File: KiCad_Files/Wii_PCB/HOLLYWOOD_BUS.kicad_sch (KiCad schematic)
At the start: 5 parts

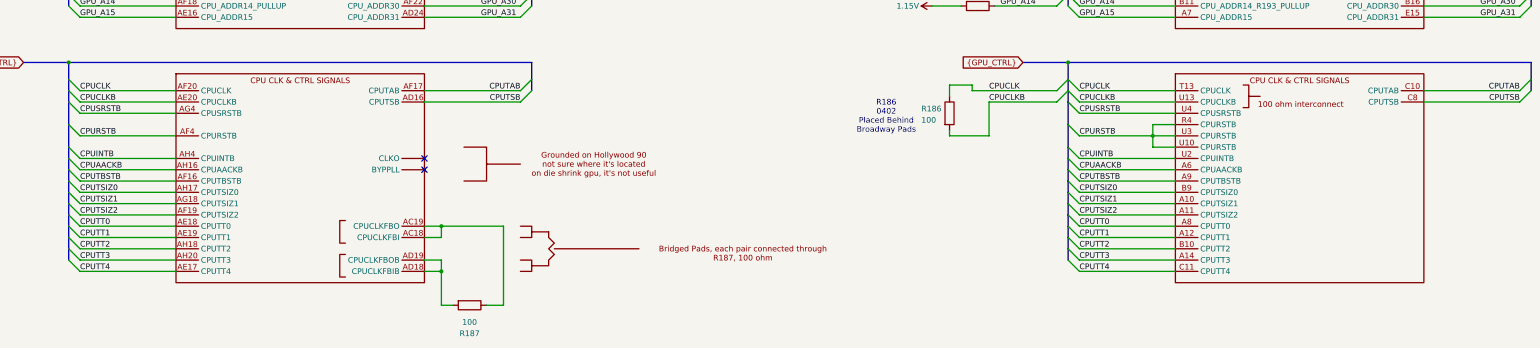
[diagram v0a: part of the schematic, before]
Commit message: Updated RAM & GPU bus to allow custom net rules for measuring intra-track spacing, added pad for reset, removed debug pads, reorganized ram schematic to cluster length matched signals, changed MX chip and U10 symbols, and re-labeled the wifi net interface.
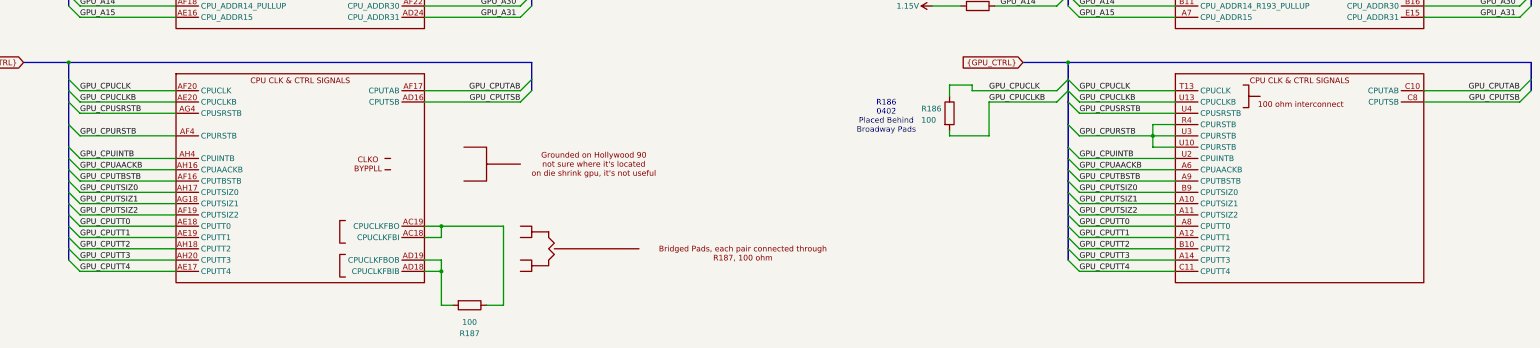
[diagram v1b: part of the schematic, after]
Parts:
- BROADWAY1: footprint wii_bgaLibrary:Updated BROADWAY -> WeeWii_Library:Updated BROADWAY
- HOLLYWOOD1: footprint wii_bgaLibrary:Updated HOLLYWOOD -> WeeWii_Library:Updated HOLLYWOOD
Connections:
- net CPUAACKB renamed GPU_CPUAACKB
- net CPUCLK renamed GPU_CPUCLK
- net CPUCLKB renamed GPU_CPUCLKB
- net CPUINTB renamed GPU_CPUINTB
- net CPURSTB renamed GPU_CPURSTB
- net CPUSRSTB renamed GPU_CPUSRSTB
- net CPUTAB renamed GPU_CPUTAB
- net CPUTBSTB renamed GPU_CPUTBSTB
- net CPUTSB renamed GPU_CPUTSB
- net CPUTSIZ0 renamed GPU_CPUTSIZ0
- net CPUTSIZ1 renamed GPU_CPUTSIZ1
- net CPUTSIZ2 renamed GPU_CPUTSIZ2
- net CPUTT0 renamed GPU_CPUTT0
- net CPUTT1 renamed GPU_CPUTT1
- net CPUTT2 renamed GPU_CPUTT2
- net CPUTT3 renamed GPU_CPUTT3
- net CPUTT4 renamed GPU_CPUTT4
- no-connect marks 2 -> 0
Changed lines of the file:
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@@
 	(paper "A3")
 	(bus_alias "GPU_CTRL"
-		(members "CPUCLK" "CPUCLKB" "CPUSRSTB" "CPURSTB" "CPUINTB" "CPUAACKB" "CPUTBSTB"
-			"CPUTSIZ0" "CPUTSIZ1" "CPUTSIZ2" "CPUTT0" "CPUTT1" "CPUTT2" "CPUTT3" "CPUTT4"
-			"CPUTAB" "CPUTSB"
+		(members "GPU_CPUCLK" "GPU_CPUCLKB" "GPU_CPUSRSTB" "GPU_CPURSTB" "GPU_CPUINTB"
+			"GPU_CPUAACKB" "GPU_CPUTBSTB" "GPU_CPUTSIZ0" "GPU_CPUTSIZ1" "GPU_CPUTSIZ2"
+			"GPU_CPUTT0" "GPU_CPUTT1" "GPU_CPUTT2" "GPU_CPUTT3" "GPU_CPUTT4" "GPU_CPUTAB"
+			"GPU_CPUTSB"
 		)
 	)
@@
 		(color 0 0 0 0)
 	)
-	(no_connect
-		(at 132.08 222.25)
-	)
-	(no_connect
-		(at 132.08 224.79)
-	)
 	(bus_entry
 		(at 378.46 180.34)
@@
 		)
 	)
-	(label "CPUTSB"
+	(label "GPU_CPUTSB"
 		(at 378.46 209.55 180)
 		(effects
@@
 		)
 	)
-	(label "CPUTSIZ2"
+	(label "GPU_CPUTSIZ2"
 		(at 279.4 234.95 0)
 		(effects
@@
 		)
 	)
-	(label "CPUTT4"
+	(label "GPU_CPUTT4"
 		(at 54.61 247.65 0)
 		(effects
@@
 		)
 	)
-	(label "CPUTBSTB"
+	(label "GPU_CPUTBSTB"
 		(at 54.61 227.33 0)
 		(effects
@@
 		)
 	)
-	(label "CPUAACKB"
+	(label "GPU_CPUAACKB"
 		(at 279.4 224.79 0)
 		(effects
@@
 		)
 	)
-	(label "CPUCLKB"
+	(label "GPU_CPUCLKB"
 		(at 279.4 209.55 0)
 		(effects
@@
 		)
 	)
-	(label "CPUTT1"
+	(label "GPU_CPUTT1"
 		(at 279.4 240.03 0)
 		(effects
@@
 		)
 	)
-	(label "CPUCLK"
+	(label "GPU_CPUCLK"
 		(at 54.61 207.01 0)
 		(effects
@@
 		)
 	)
-	(label "CPUSRSTB"
+	(label "GPU_CPUSRSTB"
 		(at 279.4 212.09 0)
 		(effects
@@
 		)
 	)
-	(label "CPURSTB"
+	(label "GPU_CPURSTB"
 		(at 54.61 217.17 0)
 		(effects
@@
 		)
 	)
-	(label "CPURSTB"
+	(label "GPU_CPURSTB"
 		(at 279.4 217.17 0)
 		(effects
@@
 		)
 	)
-	(label "CPUTT1"
+	(label "GPU_CPUTT1"
 		(at 54.61 240.03 0)
 		(effects
@@
 		)
 	)
-	(label "CPUTSB"
+	(label "GPU_CPUTSB"
 		(at 153.67 209.55 180)
 		(effects
@@
 		)
 	)
-	(label "CPUCLKB"
+	(label "GPU_CPUCLKB"
 		(at 54.61 209.55 0)
 		(effects
@@
 		)
 	)
-	(label "CPUINTB"
+	(label "GPU_CPUINTB"
 		(at 54.61 222.25 0)
 		(effects
@@
 		)
 	)
-	(label "CPUSRSTB"
+	(label "GPU_CPUSRSTB"
 		(at 54.61 212.09 0)
 		(effects
@@
 		)
 	)
-	(label "CPUTSIZ2"
+	(label "GPU_CPUTSIZ2"
 		(at 54.61 234.95 0)
 		(effects
@@
 		)
 	)
-	(label "CPUTSIZ0"
+	(label "GPU_CPUTSIZ0"
 		(at 54.61 229.87 0)
 		(effects
@@
 		)
 	)
-	(label "CPUTT2"
+	(label "GPU_CPUTT2"
 		(at 279.4 242.57 0)
 		(effects
@@
 		)
 	)
-	(label "CPUTSIZ1"
+	(label "GPU_CPUTSIZ1"
 		(at 279.4 232.41 0)
 		(effects
@@
 		)
 	)
-	(label "CPUTBSTB"
+	(label "GPU_CPUTBSTB"
 		(at 279.4 227.33 0)
 		(effects
@@
 		)
 	)
-	(label "CPUTT3"
+	(label "GPU_CPUTT3"
 		(at 54.61 245.11 0)
 		(effects
@@
 		)
 	)
-	(label "CPUTT4"
+	(label "GPU_CPUTT4"
 		(at 279.4 247.65 0)
 		(effects
@@
 		)
 	)
-	(label "CPUCLKB"
+	(label "GPU_CPUCLKB"
 		(at 259.08 209.55 0)
 		(effects
@@
 		)
 	)
-	(label "CPUTT0"
+	(label "GPU_CPUTT0"
 		(at 279.4 237.49 0)
 		(effects
@@
 		)
 	)
-	(label "CPUTSIZ0"
+	(label "GPU_CPUTSIZ0"
 		(at 279.4 229.87 0)
 		(effects
@@
 		)
 	)
-	(label "CPUTT3"
+	(label "GPU_CPUTT3"
 		(at 279.4 245.11 0)
 		(effects
@@
 		)
 	)
-	(label "CPUAACKB"
+	(label "GPU_CPUAACKB"
 		(at 54.61 224.79 0)
 		(effects
@@
 		)
 	)
-	(label "CPUTT2"
+	(label "GPU_CPUTT2"
 		(at 54.61 242.57 0)
 		(effects
@@
 		)
 	)
-	(label "CPUTAB"
+	(label "GPU_CPUTAB"
 		(at 378.46 207.01 180)
 		(effects
@@
 		)
 	)
-	(label "CPUTAB"
+	(label "GPU_CPUTAB"
 		(at 153.67 207.01 180)
 		(effects
@@
 		)
 	)
-	(label "CPUCLK"
+	(label "GPU_CPUCLK"
 		(at 259.08 207.01 0)
 		(effects
@@
 		)
 	)
-	(label "CPUINTB"
+	(label "GPU_CPUINTB"
 		(at 279.4 222.25 0)
 		(effects
@@
 		)
 	)
-	(label "CPUTSIZ1"
+	(label "GPU_CPUTSIZ1"
 		(at 54.61 232.41 0)
 		(effects
@@
 		)
 	)
-	(label "CPUCLK"
+	(label "GPU_CPUCLK"
 		(at 279.4 207.01 0)
 		(effects
@@
 		)
 	)
-	(label "CPUTT0"
+	(label "GPU_CPUTT0"
 		(at 54.61 237.49 0)
 		(effects
@@
 			)
 		)
-		(property "Footprint" "wii_bgaLibrary:Updated HOLLYWOOD"
+		(property "Footprint" "WeeWii_Library:Updated HOLLYWOOD"
 			(at 104.14 68.326 0)
 			(effects
@@
 		(pin "AD16"
 		)
-		(pin ""
-		)
-		(pin ""
+		(pin "C16"
 		)
 		(pin "AC19"
@@
 		(pin "B12"
 		)
-		(pin "C16"
-		)
 		(pin "D26"
 		)
 		(pin "C24"
 		)
-		(pin "D16"
-		)
 		(pin "U26"
 		)
@@
 		(pin "G12"
 		)
+		(pin "B14"
+		)
+		(pin "A24"
+		)
+		(pin "E14"
+		)
+		(pin "N10"
+		)
+		(pin "D19"
+		)
 		(instances
 			(project ""
@@
 			)
 		)
-		(property "Footprint" "wii_bgaLibrary:Updated BROADWAY"
+		(property "Footprint" "WeeWii_Library:Updated BROADWAY"
 			(at 328.93 55.88 0)
 			(effects
